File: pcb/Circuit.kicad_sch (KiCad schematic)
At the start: 47 parts, among them J1 DTM13-12PA-R008, J2 TSW-101-07-T-D, J3 TSW-101-07-T-D, U1 MCP1700-1802E_TO92, U2 CDP68HC68S1, U3 LM2672N-5.0, U4 Teensy4.0, U5 MCP2562-H-P

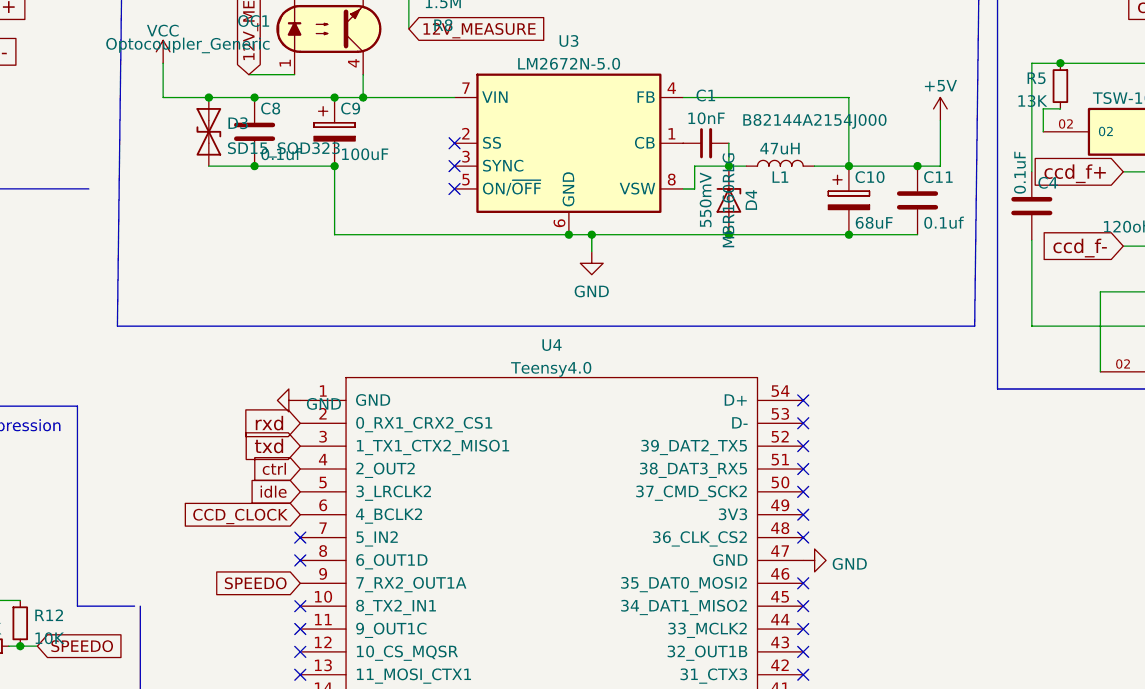
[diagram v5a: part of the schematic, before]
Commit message: Update for actual parts ordered from Mouser
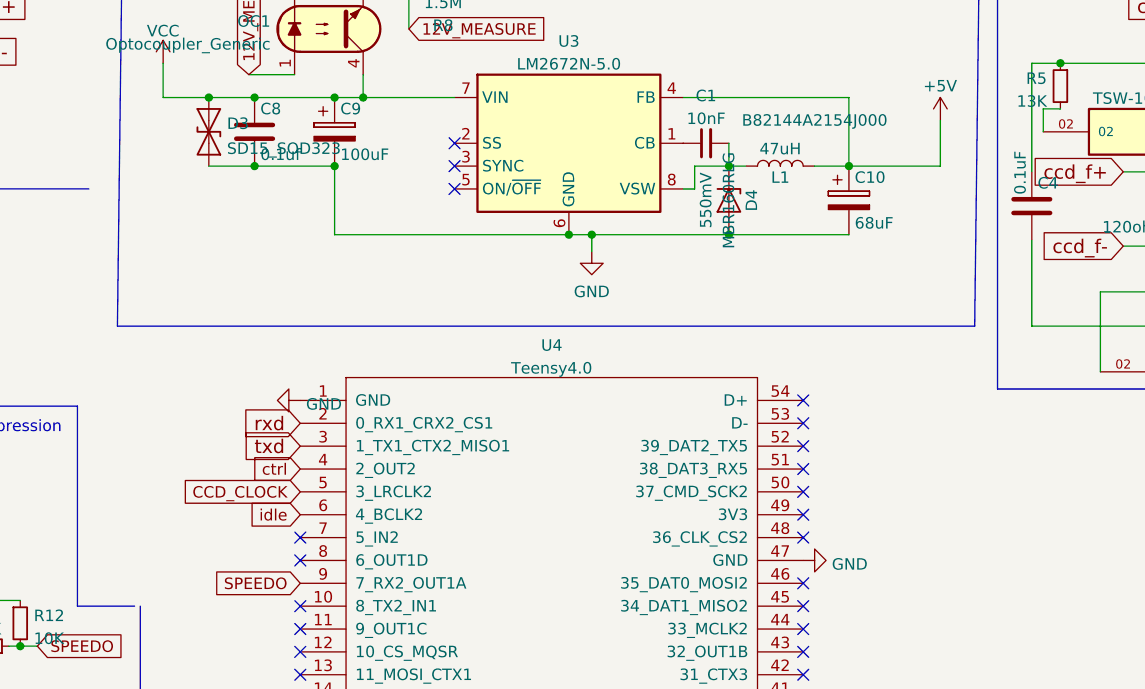
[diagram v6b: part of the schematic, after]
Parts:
- removed C11: 0.1uf, Capacitor_THT:C_Disc_D7.0mm_W2.5mm_P5.00mm, symbol ccd_can_bridge-rescue:C
- C2, C3, C4, C8: footprint Capacitor_THT:C_Disc_D7.0mm_W2.5mm_P5.00mm -> Capacitor_THT:C_Disc_D3.8mm_W2.6mm_P2.50mm
- C9: footprint Capacitor_THT:C_Disc_D7.0mm_W2.5mm_P5.00mm -> Capacitor_THT:CP_Radial_D5.0mm_P2.50mm
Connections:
- net CCD_CLOCK: now also U4.5 (3_LRCLK2); no longer U4.6 (4_BCLK2)
- net idle: now also U4.6 (4_BCLK2); no longer U4.5 (3_LRCLK2)
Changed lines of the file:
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@@
   (junction (at 52.705 104.775) (diameter 0) (color 0 0 0 0)
   )
-  (junction (at 173.99 51.435) (diameter 0) (color 0 0 0 0)
-  )
   (junction (at 255.905 40.005) (diameter 0) (color 0 0 0 0)
   )
@@
   )
   (junction (at 36.195 57.15) (diameter 0) (color 0 0 0 0)
-  )
-  (junction (at 166.37 59.055) (diameter 0) (color 0 0 0 0)
   )
   (no_connect (at 161.29 125.73))
@@
     (stroke (width 0) (type default) (color 0 0 0 0))
   )
-  (wire (pts (xy 173.99 51.435) (xy 166.37 51.435))
-    (stroke (width 0) (type default) (color 0 0 0 0))
-  )
   (wire (pts (xy 222.885 52.07) (xy 226.06 55.245))
     (stroke (width 0) (type default) (color 0 0 0 0))
@@
     (stroke (width 0) (type default) (color 0 0 0 0))
   )
-  (wire (pts (xy 173.99 59.055) (xy 166.37 59.055))
-    (stroke (width 0) (type default) (color 0 0 0 0))
-  )
   (wire (pts (xy 211.455 33.655) (xy 218.44 33.655))
     (stroke (width 0) (type default) (color 0 0 0 0))
@@
     (stroke (width 0) (type default) (color 0 0 0 0))
   )
-  (wire (pts (xy 176.53 51.435) (xy 173.99 51.435))
+  (wire (pts (xy 166.37 51.435) (xy 176.53 51.435))
     (stroke (width 0) (type default) (color 0 0 0 0))
   )
@@
     )
   )
-  (global_label "idle" (shape input) (at 105.41 87.63 180) (fields_autoplaced)
+  (global_label "idle" (shape input) (at 105.41 90.17 180) (fields_autoplaced)
     (effects (font (size 1.27 1.27)) (justify right))
-    (property "Intersheet References" "${INTERSHEET_REFS}" (id 0) (at 99.4893 87.5506 0)
+    (property "Intersheet References" "${INTERSHEET_REFS}" (id 0) (at 99.4893 90.0906 0)
       (effects (font (size 1.27 1.27)) (justify right) hide)
     )
@@
     )
   )
-  (global_label "CCD_CLOCK" (shape input) (at 105.41 90.17 180) (fields_autoplaced)
+  (global_label "CCD_CLOCK" (shape input) (at 105.41 87.63 180) (fields_autoplaced)
     (effects (font (size 1.27 1.27)) (justify right))
-    (property "Intersheet References" "${INTERSHEET_REFS}" (id 0) (at 92.0507 90.0906 0)
+    (property "Intersheet References" "${INTERSHEET_REFS}" (id 0) (at 92.0507 87.5506 0)
       (effects (font (size 1.27 1.27)) (justify right) hide)
     )
@@
       (effects (font (size 1.27 1.27)) (justify left))
     )
-    (property "Footprint" "Capacitor_THT:C_Disc_D7.0mm_W2.5mm_P5.00mm" (id 2) (at 101.2952 51.435 0)
+    (property "Footprint" "Capacitor_THT:C_Disc_D3.8mm_W2.6mm_P2.50mm" (id 2) (at 101.2952 51.435 0)
       (effects (font (size 1.27 1.27)) hide)
     )
@@
       (effects (font (size 1.27 1.27)) (justify left))
     )
-    (property "Footprint" "Capacitor_THT:C_Disc_D7.0mm_W2.5mm_P5.00mm" (id 2) (at 187.6552 59.69 0)
+    (property "Footprint" "Capacitor_THT:C_Disc_D3.8mm_W2.6mm_P2.50mm" (id 2) (at 187.6552 59.69 0)
       (effects (font (size 1.27 1.27)) hide)
     )
@@
       (effects (font (size 1.27 1.27)) (justify left))
     )
-    (property "Footprint" "Capacitor_THT:C_Disc_D7.0mm_W2.5mm_P5.00mm" (id 2) (at 275.2852 53.975 0)
+    (property "Footprint" "Capacitor_THT:C_Disc_D3.8mm_W2.6mm_P2.50mm" (id 2) (at 275.2852 53.975 0)
       (effects (font (size 1.27 1.27)) hide)
     )
@@
       (effects (font (size 1.27 1.27)) (justify left))
     )
-    (property "Footprint" "Capacitor_THT:C_Disc_D7.0mm_W2.5mm_P5.00mm" (id 2) (at 110.1852 51.435 0)
+    (property "Footprint" "Capacitor_THT:CP_Radial_D5.0mm_P2.50mm" (id 2) (at 110.1852 51.435 0)
       (effects (font (size 1.27 1.27)) hide)
     )
@@
       (effects (font (size 1.27 1.27)) (justify left))
     )
-    (property "Footprint" "Capacitor_THT:C_Disc_D7.0mm_W2.5mm_P5.00mm" (id 2) (at 49.8602 57.15 0)
+    (property "Footprint" "Capacitor_THT:C_Disc_D3.8mm_W2.6mm_P2.50mm" (id 2) (at 49.8602 57.15 0)
       (effects (font (size 1.27 1.27)) hide)
     )
@@
     (pin "02")
   )
-  (symbol (lib_id "ccd_can_bridge-rescue:C") (at 173.99 55.245 0) (unit 1)
-    (in_bom yes) (on_board yes)
-    (property "Reference" "C11" (id 0) (at 174.625 52.705 0)
-      (effects (font (size 1.27 1.27)) (justify left))
-    )
-    (property "Value" "0.1uf" (id 1) (at 174.625 57.785 0)
-      (effects (font (size 1.27 1.27)) (justify left))
-    )
-    (property "Footprint" "Capacitor_THT:C_Disc_D7.0mm_W2.5mm_P5.00mm" (id 2) (at 174.9552 59.055 0)
-      (effects (font (size 1.27 1.27)) hide)
-    )
-    (property "Datasheet" "" (id 3) (at 173.99 55.245 0))
-    (pin "1")
-    (pin "2")
-  )
   (symbol (lib_id "Device:C_Small") (at 222.885 55.88 0) (mirror y) (unit 1)
     (in_bom yes) (on_board yes) (fields_autoplaced)
@@
     )
     (path "/d1675de1-96a6-4e2f-926f-dc005f79a17e"
-      (reference "C2") (unit 1) (value "0.1uF") (footprint "Capacitor_THT:C_Disc_D7.0mm_W2.5mm_P5.00mm")
+      (reference "C2") (unit 1) (value "0.1uF") (footprint "Capacitor_THT:C_Disc_D3.8mm_W2.6mm_P2.50mm")
     )
     (path "/ac270c6a-2006-41aa-8cc2-735e97fd3793"
-      (reference "C3") (unit 1) (value "0.1uF") (footprint "Capacitor_THT:C_Disc_D7.0mm_W2.5mm_P5.00mm")
+      (reference "C3") (unit 1) (value "0.1uF") (footprint "Capacitor_THT:C_Disc_D3.8mm_W2.6mm_P2.50mm")
     )
     (path "/804eea12-a6fe-4bad-82ea-13fafde4e6a5"
-      (reference "C4") (unit 1) (value "0.1uF") (footprint "Capacitor_THT:C_Disc_D7.0mm_W2.5mm_P5.00mm")
+      (reference "C4") (unit 1) (value "0.1uF") (footprint "Capacitor_THT:C_Disc_D3.8mm_W2.6mm_P2.50mm")
     )
     (path "/e2fe818b-e894-4111-8113-28ecb3a892a1"
@@
     )
     (path "/5fa393d1-bc57-4048-a1c8-accb336b4802"
-      (reference "C8") (unit 1) (value "0.1uf") (footprint "Capacitor_THT:C_Disc_D7.0mm_W2.5mm_P5.00mm")
+      (reference "C8") (unit 1) (value "0.1uf") (footprint "Capacitor_THT:C_Disc_D3.8mm_W2.6mm_P2.50mm")
     )
     (path "/cb7c1e3e-a32d-43a8-bf93-cbb15668bf6c"
-      (reference "C9") (unit 1) (value "100uF") (footprint "Capacitor_THT:C_Disc_D7.0mm_W2.5mm_P5.00mm")
+      (reference "C9") (unit 1) (value "100uF") (footprint "Capacitor_THT:CP_Radial_D5.0mm_P2.50mm")
     )
     (path "/94102ff7-de7c-415b-a1d0-291d8e746d24"
       (reference "C10") (unit 1) (value "68uF") (footprint "Capacitor_THT:C_Radial_D5.0mm_H11.0mm_P2.00mm")
     )
-    (path "/dff99b7d-44b4-4c8b-a979-a916e87bc0d1"
-      (reference "C11") (unit 1) (value "0.1uf") (footprint "Capacitor_THT:C_Disc_D7.0mm_W2.5mm_P5.00mm")
-    )
     (path "/f9ff434f-6fda-4e8a-b02b-cc2fe6dec8ab"

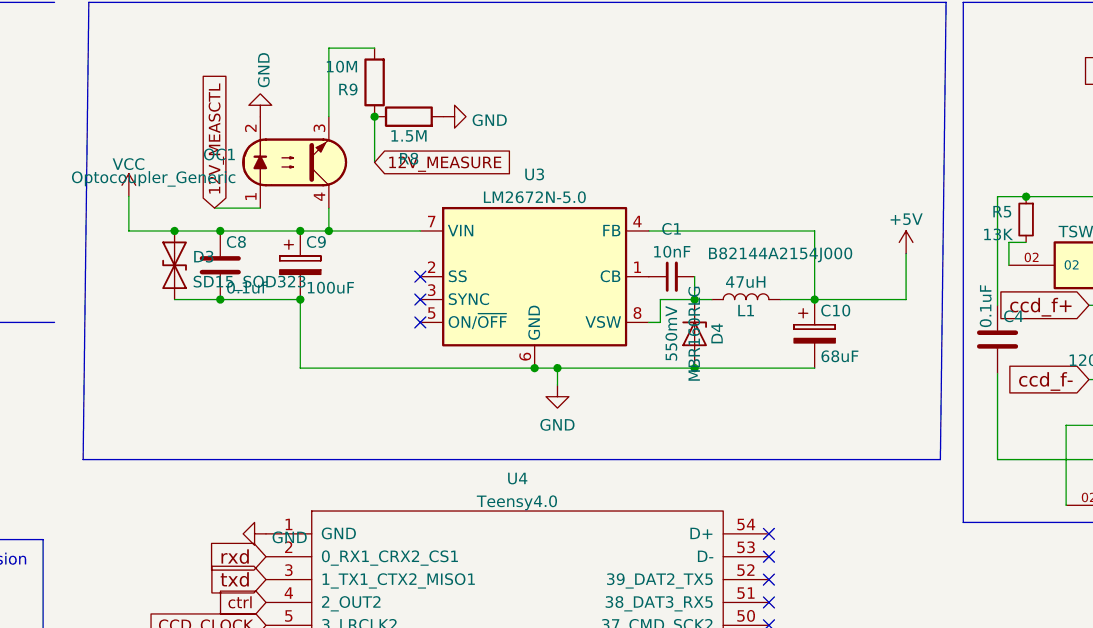
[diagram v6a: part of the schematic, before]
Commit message: Circuit using LM2591HVT
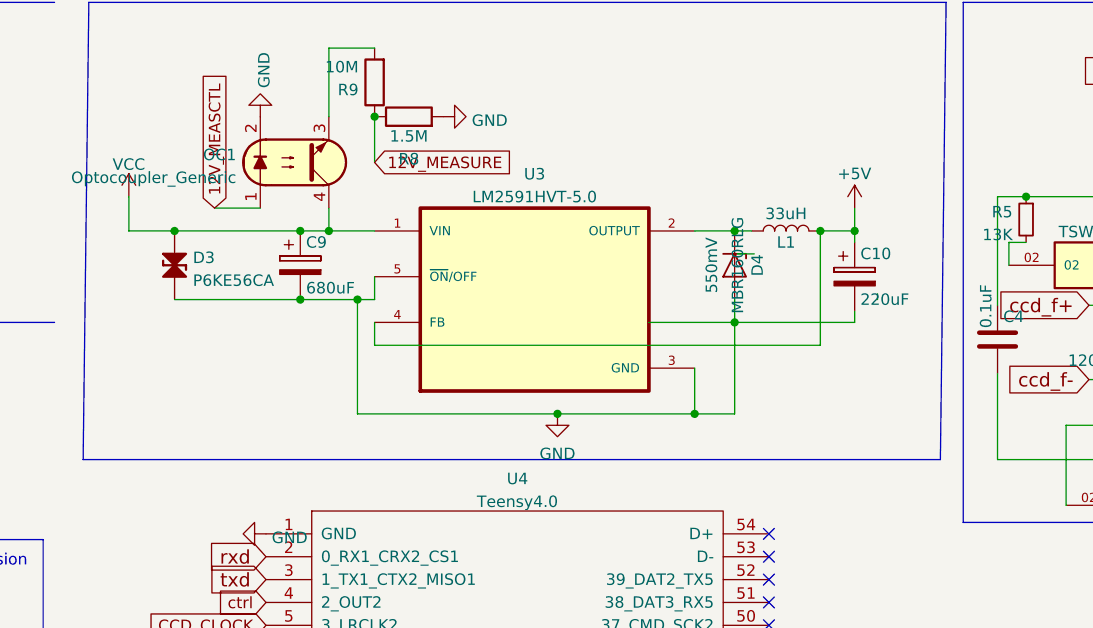
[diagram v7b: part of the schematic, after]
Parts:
- removed C1: 10nF, Capacitor_THT:C_Radial_D5.0mm_H11.0mm_P2.00mm, symbol Device:C_Small
- removed C8: 0.1uf, Capacitor_THT:C_Disc_D3.8mm_W2.6mm_P2.50mm, symbol ccd_can_bridge-rescue:C
- removed D3: SD15_SOD323, Diode_THT:D_A-405_P7.62mm_Horizontal, symbol Diode:SD15_SOD323
- removed U3: LM2672N-5.0, Package_DIP:DIP-8_W7.62mm, symbol Regulator_Switching:LM2672N-5.0
- added D3: P6KE56CA, Diode_THT:D_DO-15_P10.16mm_Horizontal, symbol Diode_TVS_AKL:P6KE56CA
- added U3: LM2591HVT-5.0, TO170P1016X470X2092-5, symbol LM2591HVT-5.0:LM2591HVT-5.0
- C10: value 68uF -> 220uF
- C9: value 100uF -> 680uF
- L1: value 47uH -> 33uH
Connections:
- net +12V: now also D3.2 (A), U3.1 (VIN)
- net +5V: now also U3.4 (FB)
- net GND: now also D3.1 (K), U3.3 (GND), U3.5 (~{ON}/OFF)
- net at D4.1 (K), L1.1: now also U3.2 (OUTPUT)
- no-connect marks 39 -> 36
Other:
- moved on the sheet: C10, D4, L1
